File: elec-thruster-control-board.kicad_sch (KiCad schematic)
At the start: 44 parts, among them J1 Conn_01x02_Socket, J11 Conn_01x02_Socket, J13 Conn_02x05_Counter_Clockwise, J14 Conn_01x02_Socket, J2 Conn_01x02_Socket, J3 Conn_01x02_Socket, J4 Conn_01x02_Socket, J5 Conn_01x02_Socket, J6 Conn_01x02_Socket, J7 Conn_01x02_Socket, J8 Conn_01x02_Socket

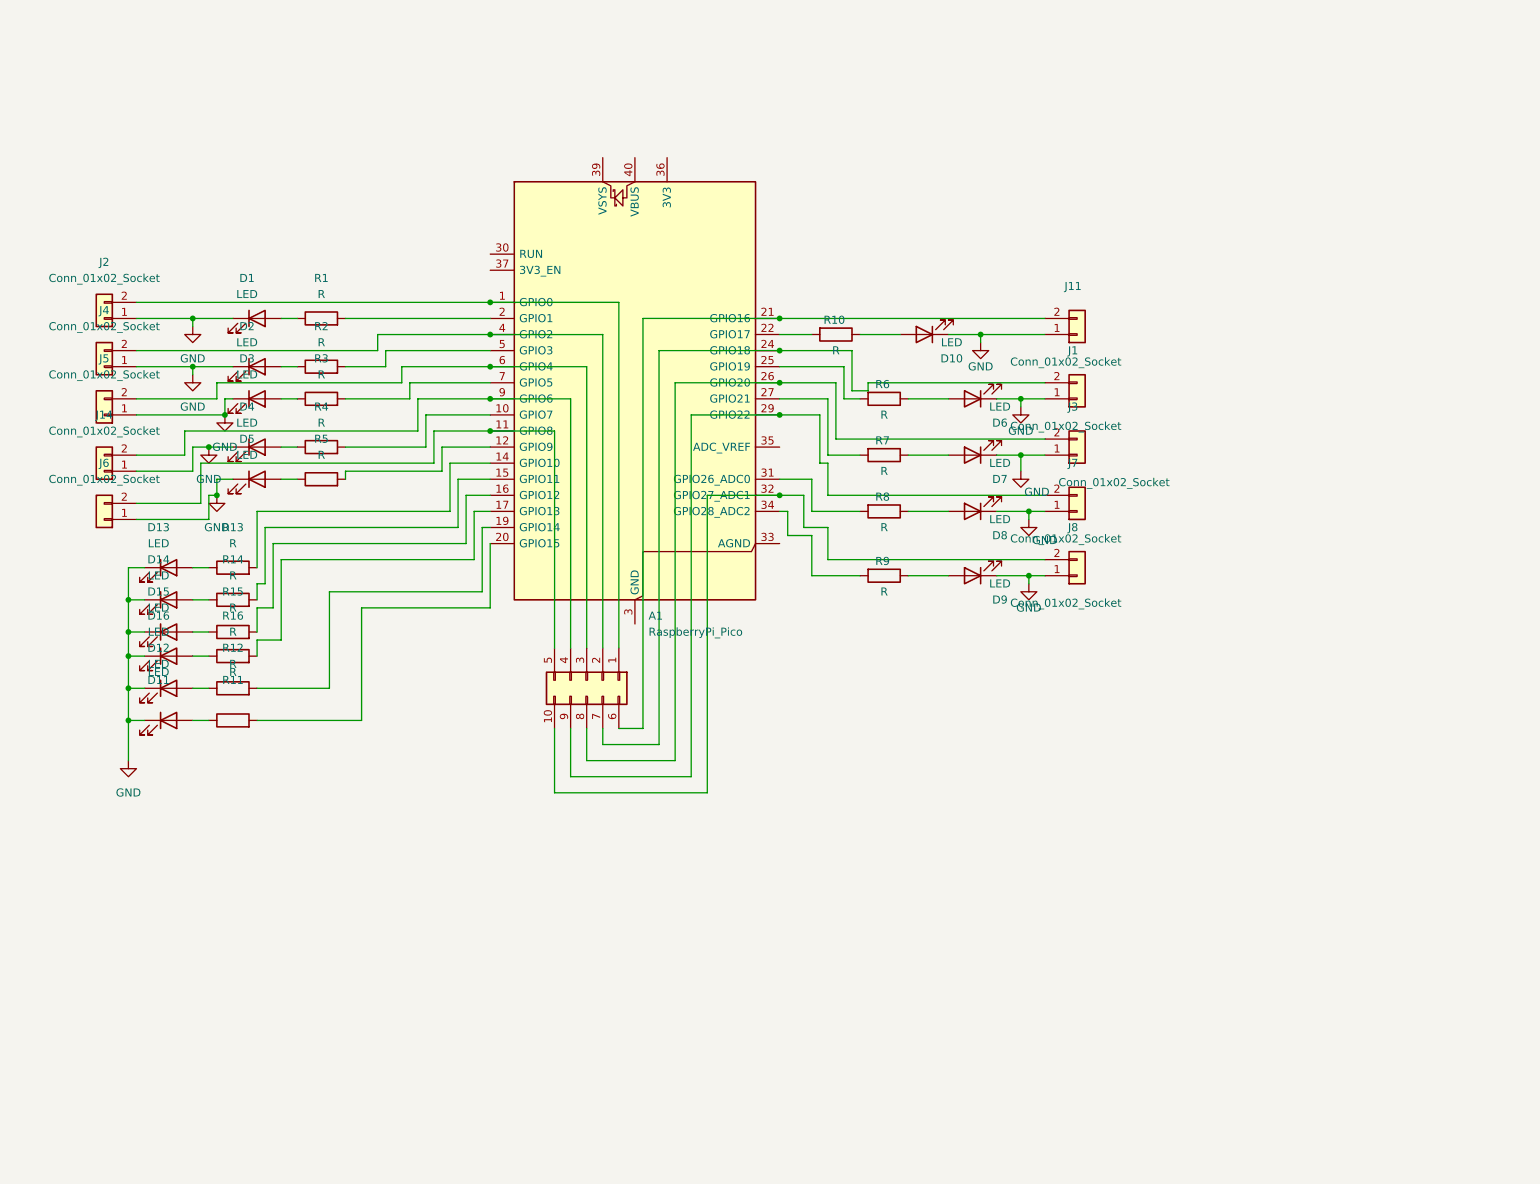
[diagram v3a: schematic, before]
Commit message: Removed overlap of labels, added single test connectors next to each pwm, fixed breakout header to fit with 8input logic analyzer
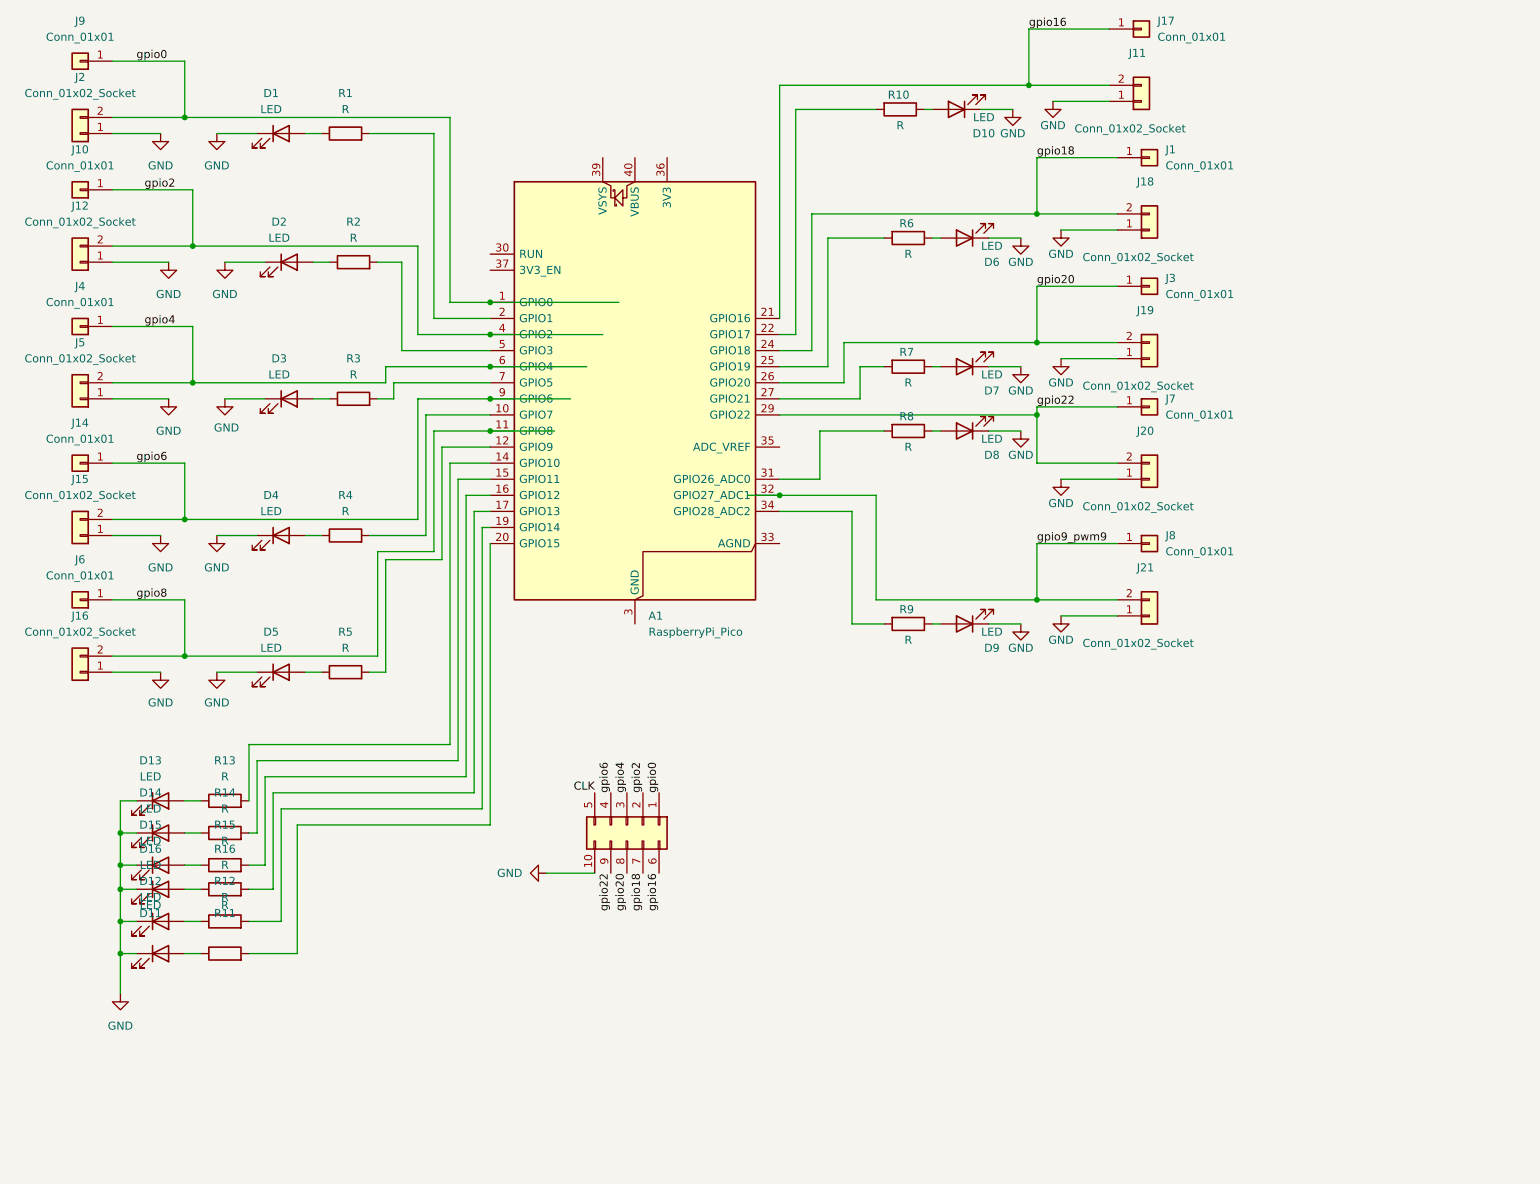
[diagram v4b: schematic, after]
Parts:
- removed J1, J14, J3, J4, J6, J7, J8: Conn_01x02_Socket, Connector_JST:JST_GH_BM02B-GHS-TBT_1x02-1MP_P1.25mm_Vertical, symbol Connector_Generic:Conn_01x02
- added J1, J10, J14, J17, J3, J4, J6, J7, J8, J9: Conn_01x01, symbol Connector_Generic:Conn_01x01
- added J12, J15, J16, J18, J19, J20, J21: Conn_01x02_Socket, Connector_JST:JST_GH_BM02B-GHS-TBT_1x02-1MP_P1.25mm_Vertical, symbol Connector_Generic:Conn_01x02
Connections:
- net GND: now also J13.10 (Pin_6), J12.1 (Pin_1), J15.1 (Pin_1), J16.1 (Pin_1), J18.1 (Pin_1), J19.1 (Pin_1), J20.1 (Pin_1), J21.1 (Pin_1)
- net gpio2: now reaches A1.4 (GPIO2), J13.2 (Pin_2)
- net gpio2: now also J10.1 (Pin_1), J12.2 (Pin_2)
- net gpio16: now reaches A1.21 (GPIO16), J11.2 (Pin_2), J13.6 (Pin_10)
- net gpio16: now also J17.1 (Pin_1)
- net gpio0: now reaches A1.1 (GPIO0), J13.1 (Pin_1), J2.2 (Pin_2)
- net gpio0: now also J9.1 (Pin_1)
- net CLK: now reaches J13.5 (Pin_5)
- net CLK: no longer A1.11 (GPIO8)
- net gpio18: now reaches A1.24 (GPIO18), J13.7 (Pin_9)
- net gpio18: now also J1.1 (Pin_1), J18.2 (Pin_2)
- net gpio20: now reaches A1.26 (GPIO20), J13.8 (Pin_8)
- net gpio20: now also J19.2 (Pin_2), J3.1 (Pin_1)
- net gpio22: now reaches A1.29 (GPIO22), J13.9 (Pin_7)
- net gpio22: now also J20.2 (Pin_2), J7.1 (Pin_1)
- net gpio9_pwm9: now reaches A1.32 (GPIO27_ADC1)
- net gpio9_pwm9: now also J21.2 (Pin_2), J8.1 (Pin_1); no longer J13.10 (Pin_6)
- net gpio4: now reaches A1.6 (GPIO4), J13.3 (Pin_3), J5.2 (Pin_2)
- net gpio4: now also J4.1 (Pin_1)
- net gpio6: now reaches A1.9 (GPIO6), J13.4 (Pin_4)
- net gpio6: now also J14.1 (Pin_1), J15.2 (Pin_2)
- new net gpio8: A1.11 (GPIO8), J16.2 (Pin_2), J6.1 (Pin_1)
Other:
- moved on the sheet: D1, D10, D11, D12, D13, D14, D15, D16, J11, J2, R1, R10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

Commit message: Removed extra LED overlap, redid wiring to separate connectors connected to identical pwm channels, labeled pwm channels
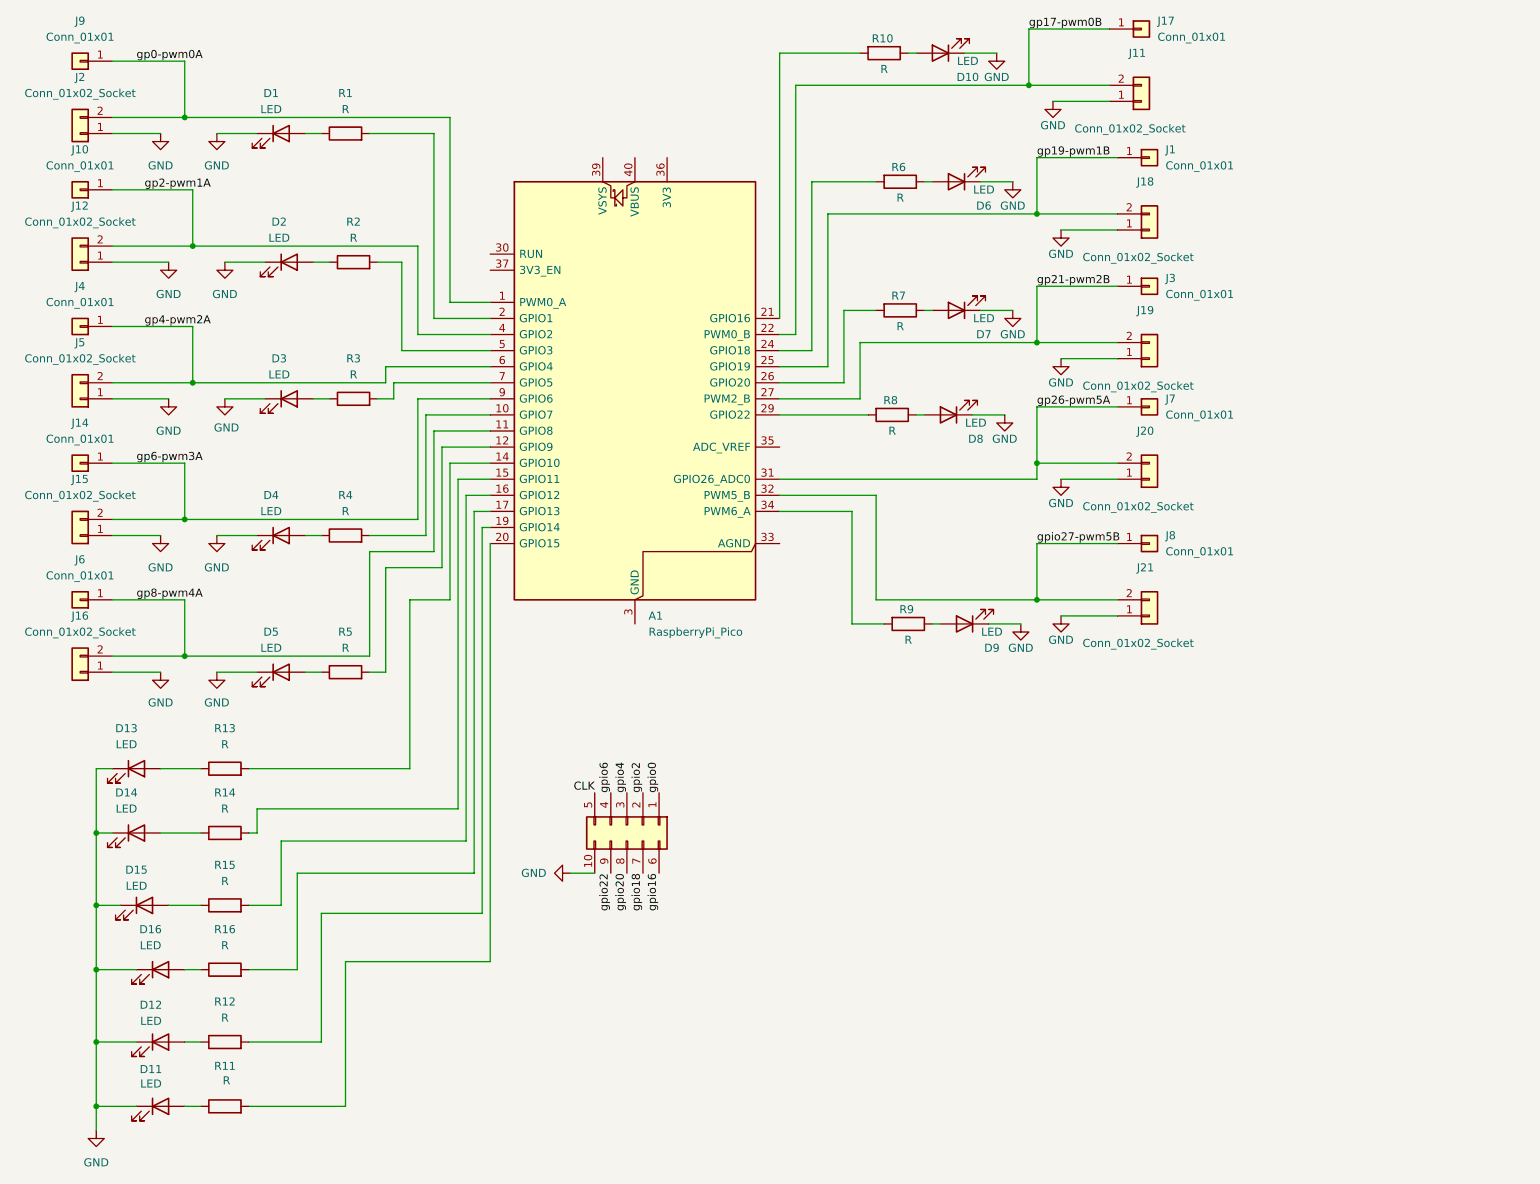
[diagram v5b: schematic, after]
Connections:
- net gpio0: no longer A1.1 (GPIO0), J2.2 (Pin_2), J9.1 (Pin_1)
- net gpio16: no longer A1.21 (GPIO16), J11.2 (Pin_2), J17.1 (Pin_1)
- net gpio18: no longer A1.24 (GPIO18), J1.1 (Pin_1), J18.2 (Pin_2)
- net gpio2: no longer A1.4 (GPIO2), J10.1 (Pin_1), J12.2 (Pin_2)
- net gpio20: no longer A1.26 (GPIO20), J19.2 (Pin_2), J3.1 (Pin_1)
- net gpio22: no longer A1.29 (GPIO22), J20.2 (Pin_2), J7.1 (Pin_1)
- net gpio4: no longer A1.6 (GPIO4), J4.1 (Pin_1), J5.2 (Pin_2)
- net gpio6: no longer A1.9 (GPIO6), J14.1 (Pin_1), J15.2 (Pin_2)
- net at R10.2: now also A1.21 (GPIO16); no longer A1.22 (GPIO17)
- net at R6.2: now also A1.24 (GPIO18); no longer A1.25 (GPIO19)
- net at R7.2: now also A1.26 (GPIO20); no longer A1.27 (GPIO21)
- net at R8.2: now also A1.29 (GPIO22); no longer A1.31 (GPIO26_ADC0)
- net gpio8 renamed gp8-pwm4A
- net gpio9_pwm9 renamed gpio27-pwm5B
- new net gp0-pwm0A: A1.1 (GPIO0), J2.2 (Pin_2), J9.1 (Pin_1)
- new net gp17-pwm0B: A1.22 (GPIO17), J11.2 (Pin_2), J17.1 (Pin_1)
- new net gp19-pwm1B: A1.25 (GPIO19), J1.1 (Pin_1), J18.2 (Pin_2)
- new net gp2-pwm1A: A1.4 (GPIO2), J10.1 (Pin_1), J12.2 (Pin_2)
- new net gp21-pwm2B: A1.27 (GPIO21), J19.2 (Pin_2), J3.1 (Pin_1)
- new net gp26-pwm5A: A1.31 (GPIO26_ADC0), J20.2 (Pin_2), J7.1 (Pin_1)
- new net gp4-pwm2A: A1.6 (GPIO4), J4.1 (Pin_1), J5.2 (Pin_2)
- new net gp6-pwm3A: A1.9 (GPIO6), J14.1 (Pin_1), J15.2 (Pin_2)
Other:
- moved on the sheet: D10, D11, D12, D13, D14, D15, D16, D6, D7, D8, R10, R11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

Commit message: fixed labels
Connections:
- net gpio0 is gone; now on net gp0-pwm0A: J13.1 (Pin_1)
- net gpio16 is gone; now on net gp17-pwm0B: J13.6 (Pin_10)
- net gpio18 is gone; now on net gp19-pwm1B: J13.7 (Pin_9)
- net gpio2 is gone; now on net gp2-pwm1A: J13.2 (Pin_2)
- net gpio20 is gone; now on net gp21-pwm2B: J13.8 (Pin_8)
- net gpio22 is gone; now on net gp26-pwm5A: J13.9 (Pin_7)
- net gpio4 is gone; now on net gp4-pwm2A: J13.3 (Pin_3)
- net gpio6 is gone; now on net gp6-pwm3A: J13.4 (Pin_4)
- net gpio27-pwm5B renamed gp27-pwm5B
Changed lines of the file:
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@@
 		)
 	)
-	(label "gpio6"
-		(at 119.38 137.16 90)
-		(effects
-			(font
-				(size 1.27 1.27)
-			)
-			(justify left bottom)
-		)
-	)
-	(label "gpio27-pwm5B"
+	(label "gp2-pwm1A"
+		(at 124.46 137.16 90)
+		(effects
+			(font
+				(size 1.27 1.27)
+			)
+			(justify left bottom)
+		)
+	)
+	(label "gp0-pwm0A"
+		(at 127 137.16 90)
+		(effects
+			(font
+				(size 1.27 1.27)
+			)
+			(justify left bottom)
+		)
+	)
+	(label "gp27-pwm5B"
 		(at 186.69 97.79 0)
 		(effects
@@
 		)
 	)
-	(label "gpio0"
-		(at 127 137.16 90)
-		(effects
-			(font
-				(size 1.27 1.27)
-			)
-			(justify left bottom)
-		)
-	)
 	(label "gp6-pwm3A"
 		(at 44.45 85.09 0)
@@
 		)
 	)
+	(label "gp6-pwm3A"
+		(at 119.38 137.16 90)
+		(effects
+			(font
+				(size 1.27 1.27)
+			)
+			(justify left bottom)
+		)
+	)
 	(label "gp4-pwm2A"
 		(at 45.72 63.5 0)
@@
 		)
 	)
+	(label "gp4-pwm2A"
+		(at 121.92 137.16 90)
+		(effects
+			(font
+				(size 1.27 1.27)
+			)
+			(justify left bottom)
+		)
+	)
 	(label "gp26-pwm5A"
 		(at 186.69 76.2 0)
@@
 		)
 	)
-	(label "gpio20"
-		(at 121.92 149.86 270)
+	(label "gp19-pwm1B"
+		(at 124.46 149.86 270)
+		(effects
+			(font
+				(size 1.27 1.27)
+			)
+			(justify right bottom)
+		)
+	)
+	(label "gp26-pwm5A"
+		(at 119.38 149.86 270)
 		(effects
 			(font
@@
 		)
 	)
-	(label "gpio22"
-		(at 119.38 149.86 270)
-		(effects
-			(font
-				(size 1.27 1.27)
-			)
-			(justify right bottom)
-		)
-	)
-	(label "gpio16"
-		(at 127 149.86 270)
-		(effects
-			(font
-				(size 1.27 1.27)
-			)
-			(justify right bottom)
-		)
-	)
 	(label "gp0-pwm0A"
 		(at 44.45 21.59 0)
@@
 		)
 	)
-	(label "gpio18"
-		(at 124.46 149.86 270)
-		(effects
-			(font
-				(size 1.27 1.27)
-			)
-			(justify right bottom)
-		)
-	)
-	(label "gpio4"
-		(at 121.92 137.16 90)
-		(effects
-			(font
-				(size 1.27 1.27)
-			)
-			(justify left bottom)
-		)
-	)
 	(label "gp19-pwm1B"
 		(at 186.69 36.83 0)
@@
 		)
 	)
-	(label "gpio2"
-		(at 124.46 137.16 90)
-		(effects
-			(font
-				(size 1.27 1.27)
-			)
-			(justify left bottom)
-		)
-	)
 	(label "gp21-pwm2B"
 		(at 186.69 57.15 0)
@@
 		)
 	)
+	(label "gp17-pwm0B"
+		(at 127 149.86 270)
+		(effects
+			(font
+				(size 1.27 1.27)
+			)
+			(justify right bottom)
+		)
+	)
 	(label "gp2-pwm1A"
 		(at 45.72 41.91 0)
@@
 			)
 			(justify left bottom)
+		)
+	)
+	(label "gp21-pwm2B"
+		(at 121.92 149.86 270)
+		(effects
+			(font
+				(size 1.27 1.27)
+			)
+			(justify right bottom)
 		)
 	)
@@
 		)
 		(pin "1"
-			(alternate "PWM0_A")
 		)
 		(pin "17"
@@
 		)
 		(pin "34"
-			(alternate "PWM6_A")
+			(alternate "GPIO28")
 		)
 		(pin "22"
-			(alternate "PWM0_B")
 		)
 		(pin "8"
 		)
 		(pin "27"
-			(alternate "PWM2_B")
 		)
 		(pin "26"
@@
 		)
 		(pin "32"
-			(alternate "PWM5_B")
+			(alternate "GPIO27")
 		)
 		(pin "33"

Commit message: Updated design
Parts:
- removed J13: Conn_02x05_Counter_Clockwise, Connector_JST:JST_PHD_B10B-PHDSS_2x05_P2.00mm_Vertical, symbol Connector_Generic:Conn_02x05_Counter_Clockwise
- D1, D10, D11, D12, D13, D14, D15, D16, D2, D3, D4, D5, D6, D7, D8, D9: footprint LED_SMD:LED_Everlight-SMD3528_3.5x2.8mm_67-21ST -> LED_SMD:LED_0805_2012Metric
- J1, J10, J14, J17, J3, J4, J6, J7, J8, J9: footprint (none) -> Connector_PinHeader_2.54mm:PinHeader_1x01_P2.54mm_Vertical
- J11: value Conn_01x02_Socket -> gp17-pwm0B; footprint Connector_JST:JST_GH_BM02B-GHS-TBT_1x02-1MP_P1.25mm_Vertical -> Connector_JST:JST_PH_S2B-PH-K_1x02_P2.00mm_Horizontal
- J12: value Conn_01x02_Socket -> gp2-pwm1A; footprint Connector_JST:JST_GH_BM02B-GHS-TBT_1x02-1MP_P1.25mm_Vertical -> Connector_JST:JST_PH_S2B-PH-K_1x02_P2.00mm_Horizontal
- J15: value Conn_01x02_Socket -> gp6-pwm3A; footprint Connector_JST:JST_GH_BM02B-GHS-TBT_1x02-1MP_P1.25mm_Vertical -> Connector_JST:JST_PH_S2B-PH-K_1x02_P2.00mm_Horizontal
- J16: value Conn_01x02_Socket -> gp8-pwm4A; footprint Connector_JST:JST_GH_BM02B-GHS-TBT_1x02-1MP_P1.25mm_Vertical -> Connector_JST:JST_PH_S2B-PH-K_1x02_P2.00mm_Horizontal
- J18: value Conn_01x02_Socket -> gp19-pwm1B; footprint Connector_JST:JST_GH_BM02B-GHS-TBT_1x02-1MP_P1.25mm_Vertical -> Connector_JST:JST_PH_S2B-PH-K_1x02_P2.00mm_Horizontal
- J19: value Conn_01x02_Socket -> gp21-pwm2B; footprint Connector_JST:JST_GH_BM02B-GHS-TBT_1x02-1MP_P1.25mm_Vertical -> Connector_JST:JST_PH_S2B-PH-K_1x02_P2.00mm_Horizontal
- J2: value Conn_01x02_Socket -> gp0-pwm0A; footprint Connector_JST:JST_GH_BM02B-GHS-TBT_1x02-1MP_P1.25mm_Vertical -> Connector_JST:JST_PH_S2B-PH-K_1x02_P2.00mm_Horizontal
- J20: value Conn_01x02_Socket -> gp26-pwm5A; footprint Connector_JST:JST_GH_BM02B-GHS-TBT_1x02-1MP_P1.25mm_Vertical -> Connector_JST:JST_PH_S2B-PH-K_1x02_P2.00mm_Horizontal
- J21: value Conn_01x02_Socket -> gp27-pwm5B; footprint Connector_JST:JST_GH_BM02B-GHS-TBT_1x02-1MP_P1.25mm_Vertical -> Connector_JST:JST_PH_S2B-PH-K_1x02_P2.00mm_Horizontal
- J5: value Conn_01x02_Socket -> gp4-pwm2A; footprint Connector_JST:JST_GH_BM02B-GHS-TBT_1x02-1MP_P1.25mm_Vertical -> Connector_JST:JST_PH_S2B-PH-K_1x02_P2.00mm_Horizontal
- R1, R10, R11, R12, R13, R14, R15, R16, R2, R3, R4, R5, R6, R7, R8, R9: footprint Resistor_SMD:R_2010_5025Metric_Pad1.40x2.65mm_HandSolder -> Resistor_SMD:R_0805_2012Metric
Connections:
- net GND: now also A1.13 (GND), A1.18 (GND), A1.23 (GND), A1.28 (GND), A1.3 (GND), A1.33 (AGND), A1.38 (GND), A1.8 (GND)
